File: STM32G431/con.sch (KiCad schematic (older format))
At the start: 64 parts, among them J10 NTC, J11 LED, J4 GND, J5 VIN, J6 UART, J7 ENCODER, J8 HALL, J9 AIN, P1 TC2030-CTX-Tag-Connect, Q2 Q_NMOS_GSD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

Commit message: updated files
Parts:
- removed D18, D19: SS310, Diode_SMD:D_SOD-123F, symbol Device:D_Small
- removed J7: ENCODER, Connector_Molex:Molex_PicoBlade_53261-0671_1x06-1MP_P1.25mm_Horizontal, symbol Connector_Generic_MountingPin:Conn_01x06_MountingPin
- removed J9: AIN, Connector_Molex:Molex_PicoBlade_53261-0371_1x03-1MP_P1.25mm_Horizontal, symbol Connector_Generic_MountingPin:Conn_01x03_MountingPin
- removed R18, R22: 120, Resistor_SMD:R_0603_1608Metric, symbol Device:R_Small
- removed U6: ENCODER A, Package_SO:SOIC-8_3.9x4.9mm_P1.27mm, symbol otter:RS485
- removed U7: ENCODER B, Package_SO:SOIC-8_3.9x4.9mm_P1.27mm, symbol otter:RS485
- added D14, D15: SM4007PL, Diode_SMD:D_SOD-123F, symbol Device:D_Small
- added D2, D5: B5819W, Diode_SMD:D_SOD-123, symbol Device:D_Schottky
- added J9: AIN/PWM, Connector_Molex:Molex_PicoBlade_53261-0471_1x04-1MP_P1.25mm_Horizontal, symbol Connector_Generic_MountingPin:Conn_01x04_MountingPin
- gave numbers to parts that had none: 4
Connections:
- net +3V3: now also D2.1 (K)
- net CANRX: no longer R5.2, U11.1 (IO1), U5.1 (DI)
- net CANTX: no longer R4.2, U11.3 (IO2), U5.4 (DO)
- net GND: now also D14.2 (A), J9.4 (Pin_4), J9.MP (MountPin); no longer R24.2
- net GPIO_BEMF: now also D5.1 (K)
- net NTC_EXT: now also D15.2 (A)
- net UU: now also R24.2, D2.2 (A); no longer R24.1
- net UV: now also D6.2 (A)
- net VIO: now also J9.1 (Pin_1)
- net at R45.2, R46.2: now also J9.3 (Pin_3)
- net at C40.1, Q2.1 (G), R21.1: now also D15.1 (K)
- net at C35.2, L1.1, U3.1 (SW): now also D14.1 (K)
- new net: D5.2 (A), R24.1
- new net PWM: J9.2 (Pin_2), U11.3 (IO2)
- new net UART_RX: R4.2, U5.4 (DO)
- new net UART_TX: R5.2, U5.1 (DI)
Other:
- moved on the sheet: C29, D10, D13, D6, D7, R23, R24, R26, R31, U5

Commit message: updated files
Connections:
- net NTC_EXT: now also U9.4 (IO3); no longer U8.6 (IO4)
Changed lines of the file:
@@
 Text GLabel 9550 3400 0    50   Input ~ 0
 SWDIO
-Text GLabel 10150 3500 2    50   Input ~ 0
+Text GLabel 10150 4300 2    50   Input ~ 0
 NTC_POWERSTAGE
 Text GLabel 10150 4900 2    50   Input ~ 0

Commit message: updated files
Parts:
- R27, R28, R29: value 100 -> 1.8k
- R33, R34, R35: value 1k -> 10k
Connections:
- net VIO is gone; now on net +3V3: J9.1 (Pin_1), JP2.1 (A), P1.1 (VCC), R33.1, R34.1, R35.1, R46.1
- net VP renamed +12V
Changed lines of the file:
@@
 AR Path="/5D59ABFE/5D5B747D" Ref="R35"  Part="1"
 F 0 "R35" H 6458 1704 50  0000 L CNN
-F 1 "1k" H 6458 1795 50  0000 L CNN
+F 1 "10k" H 6458 1795 50  0000 L CNN
 F 2 "Resistor_SMD:R_0603_1608Metric" H 6400 1750 50  0001 C CNN
 F 3 "~" H 6400 1750 50  0001 C CNN
@@
 AR Path="/5D59ABFE/5D5B7483" Ref="R34"  Part="1"
 F 0 "R34" H 6600 2100 50  0000 R CNN
-F 1 "1k" H 6550 1950 50  0000 R CNN
+F 1 "10k" H 6550 1950 50  0000 R CNN
 F 2 "Resistor_SMD:R_0603_1608Metric" H 6500 1750 50  0001 C CNN
 F 3 "~" H 6500 1750 50  0001 C CNN
@@
 AR Path="/5D59ABFE/5D5B7489" Ref="R33"  Part="1"
 F 0 "R33" H 6541 1704 50  0000 R CNN
-F 1 "1k" H 6541 1795 50  0000 R CNN
+F 1 "10k" H 6541 1795 50  0000 R CNN
 F 2 "Resistor_SMD:R_0603_1608Metric" H 6600 1750 50  0001 C CNN
 F 3 "~" H 6600 1750 50  0001 C CNN
@@
 AR Path="/5D59ABFE/5D5B757B" Ref="R28"  Part="1"
 F 0 "R28" V 6200 750 50  0000 C CNN
-F 1 "100" V 6300 750 50  0000 C CNN
+F 1 "1.8k" V 6300 750 50  0000 C CNN
 F 2 "Resistor_SMD:R_0603_1608Metric" H 6250 1200 50  0001 C CNN
 F 3 "~" H 6250 1200 50  0001 C CNN
@@
 AR Path="/5D59ABFE/5D5B7581" Ref="R27"  Part="1"
 F 0 "R27" V 6054 1100 50  0000 C CNN
-F 1 "100" V 6145 1100 50  0000 C CNN
+F 1 "1.8k" V 6145 1100 50  0000 C CNN
 F 2 "Resistor_SMD:R_0603_1608Metric" H 6250 1100 50  0001 C CNN
 F 3 "~" H 6250 1100 50  0001 C CNN
@@
 AR Path="/5D59ABFE/5D5B758B" Ref="R29"  Part="1"
 F 0 "R29" V 6354 1300 50  0000 C CNN
-F 1 "100" V 6445 1300 50  0000 C CNN
+F 1 "1.8k" V 6445 1300 50  0000 C CNN
 F 2 "Resistor_SMD:R_0603_1608Metric" H 6250 1300 50  0001 C CNN
 F 3 "~" H 6250 1300 50  0001 C CNN
@@
 Wire Wire Line
 	7700 1100 7850 1100
-Text GLabel 4850 850  0    50   Input ~ 0
-VIO
 Wire Wire Line
 	6400 1650 6400 1100
@@
 	1    0    0    -1
 $EndComp
-Text GLabel 1850 7050 0    50   Input ~ 0
-VIO
 $Comp
 L power:GND #PWR?
@@
 Text GLabel 4150 4450 1    50   Input ~ 0
 3V3
-Text GLabel 7850 900  0    50   Input ~ 0
-VIO
-Text GLabel 7700 1300 3    50   Input ~ 0
-VIO
-Text GLabel 6400 1850 3    50   Input ~ 0
-VIO
 $Comp
 L Device:R_Small R?
@@
 	1    0    0    -1
 $EndComp
-Text GLabel 3600 2850 0    50   Input ~ 0
-VP
 $Comp
 L power:GND #PWR0156
@@
 Wire Wire Line
 	4150 5200 4550 5200
+$Comp
+L power:+3.3V #PWR0212
+U 1 1 5DEBC23B
+P 6400 1900
+F 0 "#PWR0212" H 6400 1750 50  0001 C CNN
+F 1 "+3.3V" H 6415 2073 50  0000 C CNN
+F 2 "" H 6400 1900 50  0001 C CNN
+F 3 "" H 6400 1900 50  0001 C CNN
+	1    6400 1900
+	-1   0    0    1
+$EndComp
+Wire Wire Line
+	6400 1900 6400 1850
+Connection ~ 6400 1850
+$Comp
+L power:+3.3V #PWR0213
+U 1 1 5DEC0D60
+P 4850 850
+F 0 "#PWR0213" H 4850 700 50  0001 C CNN
+F 1 "+3.3V" H 4865 1023 50  0000 C CNN
+F 2 "" H 4850 850 50  0001 C CNN
+F 3 "" H 4850 850 50  0001 C CNN
+	1    4850 850
+	0    -1   -1   0
+$EndComp
+$Comp
+L power:+3.3V #PWR0214
+U 1 1 5DEC82F1
+P 7850 900
+F 0 "#PWR0214" H 7850 750 50  0001 C CNN
+F 1 "+3.3V" H 7865 1073 50  0000 C CNN
+F 2 "" H 7850 900 50  0001 C CNN
+F 3 "" H 7850 900 50  0001 C CNN
+	1    7850 900
+	0    -1   -1   0
+$EndComp
+$Comp
+L power:+3.3V #PWR0215
+U 1 1 5DEC9F93
+P 7700 1300
+F 0 "#PWR0215" H 7700 1150 50  0001 C CNN
+F 1 "+3.3V" H 7715 1473 50  0000 C CNN
+F 2 "" H 7700 1300 50  0001 C CNN
+F 3 "" H 7700 1300 50  0001 C CNN
+	1    7700 1300
+	-1   0    0    1
+$EndComp
+$Comp
+L power:+3.3V #PWR0216
+U 1 1 5DED00F0
+P 1850 7050
+F 0 "#PWR0216" H 1850 6900 50  0001 C CNN
+F 1 "+3.3V" H 1865 7223 50  0000 C CNN
+F 2 "" H 1850 7050 50  0001 C CNN
+F 3 "" H 1850 7050 50  0001 C CNN
+	1    1850 7050
+	0    -1   -1   0
+$EndComp
+$Comp
+L power:+12V #PWR0217
+U 1 1 5DED744B
+P 3600 2850
+F 0 "#PWR0217" H 3600 2700 50  0001 C CNN
+F 1 "+12V" H 3615 3023 50  0000 C CNN
+F 2 "" H 3600 2850 50  0001 C CNN
+F 3 "" H 3600 2850 50  0001 C CNN
+	1    3600 2850
+	1    0    0    -1
+$EndComp
 $EndSCHEMATC

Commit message: updated files
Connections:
- net SWDCL is gone; now on net SWCLK: U8.3 (IO2)
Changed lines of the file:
@@
 $EndComp
 Text GLabel 9550 3500 0    50   Input ~ 0
-SWDCL
+SWCLK
 Text GLabel 9550 3400 0    50   Input ~ 0
 SWDIO

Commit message: remaned files
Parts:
- removed D14, D15: SM4007PL, Diode_SMD:D_SOD-123F, symbol Device:D_Small
- added D? (x2): B5819W, Diode_SMD:D_SOD-123, symbol Device:D_Schottky
- C29, C30, C31, C42: footprint Capacitor_SMD:C_0603_1608Metric -> Capacitor_SMD:C_0402_1005Metric
- C39, C40: footprint Capacitor_SMD:C_0603_1608Metric -> Resistor_SMD:R_0402_1005Metric
- R17, R6: footprint Resistor_SMD:R_0603_1608Metric -> Capacitor_SMD:C_0402_1005Metric
- R20, R21, R27, R28, R29, R32, R33, R34, R35, R37, R38, R39, R4, R45, R46, R5: footprint Resistor_SMD:R_0603_1608Metric -> Resistor_SMD:R_0402_1005Metric
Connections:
- net 3V3 is gone; now on net +3V3: R20.1
- net GND: now also D?.2 (A)
- net NTC_EXT: now also D?.2 (A)
- net at C40.1, Q2.1 (G), R21.1: now also D?.1 (K)
- net at C35.2, L1.1, U3.1 (SW): now also D?.1 (K)
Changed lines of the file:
@@
 EESchema Schematic File Version 4
-LIBS:PAC5523-cache
+LIBS:STM32G431-cache
 EELAYER 30 0
 EELAYER END
@@
 F 0 "R35" H 6458 1704 50  0000 L CNN
 F 1 "10k" H 6458 1795 50  0000 L CNN
-F 2 "Resistor_SMD:R_0603_1608Metric" H 6400 1750 50  0001 C CNN
+F 2 "Resistor_SMD:R_0402_1005Metric" H 6400 1750 50  0001 C CNN
 F 3 "~" H 6400 1750 50  0001 C CNN
 	1    6400 1750
@@
 F 0 "R34" H 6600 2100 50  0000 R CNN
 F 1 "10k" H 6550 1950 50  0000 R CNN
-F 2 "Resistor_SMD:R_0603_1608Metric" H 6500 1750 50  0001 C CNN
+F 2 "Resistor_SMD:R_0402_1005Metric" H 6500 1750 50  0001 C CNN
 F 3 "~" H 6500 1750 50  0001 C CNN
 	1    6500 1750
@@
 F 0 "R33" H 6541 1704 50  0000 R CNN
 F 1 "10k" H 6541 1795 50  0000 R CNN
-F 2 "Resistor_SMD:R_0603_1608Metric" H 6600 1750 50  0001 C CNN
+F 2 "Resistor_SMD:R_0402_1005Metric" H 6600 1750 50  0001 C CNN
 F 3 "~" H 6600 1750 50  0001 C CNN
 	1    6600 1750
@@
 F 0 "C31" H 6092 7246 50  0000 L CNN
 F 1 "100p" H 6092 7155 50  0000 L CNN
-F 2 "Capacitor_SMD:C_0603_1608Metric" H 6000 7200 50  0001 C CNN
+F 2 "Capacitor_SMD:C_0402_1005Metric" H 6000 7200 50  0001 C CNN
 F 3 "~" H 6000 7200 50  0001 C CNN
 	1    6000 7200
@@
 F 0 "C30" H 4892 7246 50  0000 L CNN
 F 1 "100p" H 4892 7155 50  0000 L CNN
-F 2 "Capacitor_SMD:C_0603_1608Metric" H 4800 7200 50  0001 C CNN
+F 2 "Capacitor_SMD:C_0402_1005Metric" H 4800 7200 50  0001 C CNN
 F 3 "~" H 4800 7200 50  0001 C CNN
 	1    4800 7200
@@
 F 0 "C29" H 3742 7246 50  0000 L CNN
 F 1 "100p" H 3742 7155 50  0000 L CNN
-F 2 "Capacitor_SMD:C_0603_1608Metric" H 3650 7200 50  0001 C CNN
+F 2 "Capacitor_SMD:C_0402_1005Metric" H 3650 7200 50  0001 C CNN
 F 3 "~" H 3650 7200 50  0001 C CNN
 	1    3650 7200
@@
 F 0 "R39" V 3704 5200 50  0000 C CNN
 F 1 "100" V 3795 5200 50  0000 C CNN
-F 2 "Resistor_SMD:R_0603_1608Metric" H 3900 5200 50  0001 C CNN
+F 2 "Resistor_SMD:R_0402_1005Metric" H 3900 5200 50  0001 C CNN
 F 3 "~" H 3900 5200 50  0001 C CNN
 	1    3900 5200
@@
 F 0 "R28" V 6200 750 50  0000 C CNN
 F 1 "1.8k" V 6300 750 50  0000 C CNN
-F 2 "Resistor_SMD:R_0603_1608Metric" H 6250 1200 50  0001 C CNN
+F 2 "Resistor_SMD:R_0402_1005Metric" H 6250 1200 50  0001 C CNN
 F 3 "~" H 6250 1200 50  0001 C CNN
 	1    6250 1200
@@
 F 0 "R27" V 6054 1100 50  0000 C CNN
 F 1 "1.8k" V 6145 1100 50  0000 C CNN
-F 2 "Resistor_SMD:R_0603_1608Metric" H 6250 1100 50  0001 C CNN
+F 2 "Resistor_SMD:R_0402_1005Metric" H 6250 1100 50  0001 C CNN
 F 3 "~" H 6250 1100 50  0001 C CNN
 	1    6250 1100
@@
 F 0 "R29" V 6354 1300 50  0000 C CNN
 F 1 "1.8k" V 6445 1300 50  0000 C CNN
-F 2 "Resistor_SMD:R_0603_1608Metric" H 6250 1300 50  0001 C CNN
+F 2 "Resistor_SMD:R_0402_1005Metric" H 6250 1300 50  0001 C CNN
 F 3 "~" H 6250 1300 50  0001 C CNN
 	1    6250 1300
@@
 F 0 "R5" V 4304 1200 50  0000 C CNN
 F 1 "100" V 4395 1200 50  0000 C CNN
-F 2 "Resistor_SMD:R_0603_1608Metric" H 4200 1200 50  0001 C CNN
+F 2 "Resistor_SMD:R_0402_1005Metric" H 4200 1200 50  0001 C CNN
 F 3 "~" H 4200 1200 50  0001 C CNN
 	1    4200 1200
@@
 F 0 "R4" V 4004 1100 50  0000 C CNN
 F 1 "100" V 4095 1100 50  0000 C CNN
-F 2 "Resistor_SMD:R_0603_1608Metric" H 4200 1100 50  0001 C CNN
+F 2 "Resistor_SMD:R_0402_1005Metric" H 4200 1100 50  0001 C CNN
 F 3 "~" H 4200 1100 50  0001 C CNN
 	1    4200 1100
@@
 F 0 "R45" V 7304 1100 50  0000 C CNN
 F 1 "100" V 7395 1100 50  0000 C CNN
-F 2 "Resistor_SMD:R_0603_1608Metric" H 7500 1100 50  0001 C CNN
+F 2 "Resistor_SMD:R_0402_1005Metric" H 7500 1100 50  0001 C CNN
 F 3 "~" H 7500 1100 50  0001 C CNN
 	1    7500 1100
@@
 F 0 "R46" H 7750 1650 50  0000 R CNN
 F 1 "1k" H 7750 1550 50  0000 R CNN
-F 2 "Resistor_SMD:R_0603_1608Metric" H 7700 1200 50  0001 C CNN
+F 2 "Resistor_SMD:R_0402_1005Metric" H 7700 1200 50  0001 C CNN
 F 3 "~" H 7700 1200 50  0001 C CNN
 	1    7700 1200
@@
 F 0 "R21" H 5309 5346 50  0000 L CNN
 F 1 "1M" H 5309 5255 50  0000 L CNN
-F 2 "Resistor_SMD:R_0603_1608Metric" H 5250 5300 50  0001 C CNN
+F 2 "Resistor_SMD:R_0402_1005Metric" H 5250 5300 50  0001 C CNN
 F 3 "~" H 5250 5300 50  0001 C CNN
 	1    5250 5300
@@
 F 0 "C39" H 4242 5346 50  0000 L CNN
 F 1 "100p" H 4242 5255 50  0000 L CNN
-F 2 "Capacitor_SMD:C_0603_1608Metric" H 4150 5300 50  0001 C CNN
+F 2 "Resistor_SMD:R_0402_1005Metric" H 4150 5300 50  0001 C CNN
 F 3 "~" H 4150 5300 50  0001 C CNN
 	1    4150 5300
@@
 F 0 "C40" H 4992 5346 50  0000 L CNN
 F 1 "100p" H 4992 5255 50  0000 L CNN
-F 2 "Capacitor_SMD:C_0603_1608Metric" H 4900 5300 50  0001 C CNN
+F 2 "Resistor_SMD:R_0402_1005Metric" H 4900 5300 50  0001 C CNN
 F 3 "~" H 4900 5300 50  0001 C CNN
 	1    4900 5300
@@
 Connection ~ 4900 5200
 Wire Wire Line
-	4900 5200 4750 5200
+	4900 5200 4800 5200
 $Comp
 L power:GND #PWR?
@@
 F 0 "R20" H 4209 4596 50  0000 L CNN
 F 1 "47k" H 4209 4505 50  0000 L CNN
-F 2 "Resistor_SMD:R_0603_1608Metric" H 4150 4550 50  0001 C CNN
+F 2 "Resistor_SMD:R_0402_1005Metric" H 4150 4550 50  0001 C CNN
 F 3 "~" H 4150 4550 50  0001 C CNN
 	1    4150 4550
@@
 	0    -1   -1   0
 $EndComp
-Text GLabel 4150 4450 1    50   Input ~ 0
-3V3
 $Comp
 L Device:R_Small R?
@@
 F 0 "R6" H 7809 5896 50  0000 L CNN
 F 1 "100k" H 7809 5805 50  0000 L CNN
-F 2 "Resistor_SMD:R_0603_1608Metric" H 7750 5850 50  0001 C CNN
+F 2 "Capacitor_SMD:C_0402_1005Metric" H 7750 5850 50  0001 C CNN
 F 3 "~" H 7750 5850 50  0001 C CNN
 	1    7750 5850
@@
 F 0 "R17" H 7809 6196 50  0000 L CNN
 F 1 "4k3" H 7809 6105 50  0000 L CNN
-F 2 "Resistor_SMD:R_0603_1608Metric" H 7750 6150 50  0001 C CNN
+F 2 "Capacitor_SMD:C_0402_1005Metric" H 7750 6150 50  0001 C CNN
 F 3 "~" H 7750 6150 50  0001 C CNN
 	1    7750 6150
@@
 F 0 "C42" H 7542 6196 50  0000 L CNN
 F 1 "100p" H 7542 6105 50  0000 L CNN
-F 2 "Capacitor_SMD:C_0603_1608Metric" H 7450 6150 50  0001 C CNN
+F 2 "Capacitor_SMD:C_0402_1005Metric" H 7450 6150 50  0001 C CNN
 F 3 "~" H 7450 6150 50  0001 C CNN
 	1    7450 6150
@@
 F 0 "R38" H 5209 3496 50  0000 L CNN
 F 1 "9k1" H 5209 3405 50  0000 L CNN
-F 2 "Resistor_SMD:R_0603_1608Metric" H 5150 3450 50  0001 C CNN
+F 2 "Resistor_SMD:R_0402_1005Metric" H 5150 3450 50  0001 C CNN
 F 3 "~" H 5150 3450 50  0001 C CNN
 	1    5150 3450
@@
 F 0 "R37" H 5209 3196 50  0000 L CNN
 F 1 "47k" H 5209 3105 50  0000 L CNN
-F 2 "Resistor_SMD:R_0603_1608Metric" H 5150 3150 50  0001 C CNN
+F 2 "Resistor_SMD:R_0402_1005Metric" H 5150 3150 50  0001 C CNN
 F 3 "~" H 5150 3150 50  0001 C CNN
 	1    5150 3150
@@
 L power:GND #PWR0155
 U 1 1 5CEAAA67
-P 4550 3500
-F 0 "#PWR0155" H 4550 3250 50  0001 C CNN
-F 1 "GND" H 4555 3327 50  0000 C CNN
-F 2 "" H 4550 3500 50  0001 C CNN
-F 3 "" H 4550 3500 50  0001 C CNN
-	1    4550 3500
+P 4550 3600
+F 0 "#PWR0155" H 4550 3350 50  0001 C CNN
+F 1 "GND" H 4555 3427 50  0000 C CNN
+F 2 "" H 4550 3600 50  0001 C CNN
+F 3 "" H 4550 3600 50  0001 C CNN
+	1    4550 3600
 	1    0    0    -1
 $EndComp
@@
 F 0 "R32" H 1009 5196 50  0000 L CNN
 F 1 "4k3" H 1009 5105 50  0000 L CNN
-F 2 "Resistor_SMD:R_0603_1608Metric" H 950 5150 50  0001 C CNN
+F 2 "Resistor_SMD:R_0402_1005Metric" H 950 5150 50  0001 C CNN
 F 3 "~" H 950 5150 50  0001 C CNN
 	1    950  5150
@@
 UART_RX
 $Comp
-L Device:D_Small D?
-U 1 1 5DF35224
-P 4550 3400
-AR Path="/5DF35224" Ref="D?"  Part="1"
-AR Path="/5D59ABFE/5DF35224" Ref="D14"  Part="1"
-F 0 "D14" V 4504 3468 50  0000 L CNN
-F 1 "SM4007PL" V 4595 3468 50  0000 L CNN
-F 2 "Diode_SMD:D_SOD-123F" V 4550 3400 50  0001 C CNN
-F 3 "~" V 4550 3400 50  0001 C CNN
-	1    4550 3400
-	0    1    1    0
-$EndComp
-$Comp
-L Device:D_Small D?
-U 1 1 5DF3CAC5
-P 4650 5200
-AR Path="/5DF3CAC5" Ref="D?"  Part="1"
-AR Path="/5D59ABFE/5DF3CAC5" Ref="D15"  Part="1"
-F 0 "D15" V 4604 5268 50  0000 L CNN
-F 1 "SM4007PL" V 4695 5268 50  0000 L CNN
-F 2 "Diode_SMD:D_SOD-123F" V 4650 5200 50  0001 C CNN
-F 3 "~" V 4650 5200 50  0001 C CNN
-	1    4650 5200
-	-1   0    0    1
-$EndComp
-Wire Wire Line
-	4150 5200 4550 5200
-$Comp
 L power:+3.3V #PWR0212
 U 1 1 5DEBC23B
@@
 	1    0    0    -1
 $EndComp
+$Comp
+L power:+3.3V #PWR?
+U 1 1 5E0AF941
+P 4150 4450
+F 0 "#PWR?" H 4150 4300 50  0001 C CNN
+F 1 "+3.3V" H 4165 4623 50  0000 C CNN
+F 2 "" H 4150 4450 50  0001 C CNN
+F 3 "" H 4150 4450 50  0001 C CNN
+	1    4150 4450
+	1    0    0    -1
+$EndComp
+Wire Wire Line
+	4150 5200 4500 5200
+$Comp
+L Device:D_Schottky D?
+U 1 1 5DFB1AE0
+P 4650 5200
+F 0 "D?" V 4604 5279 50  0000 L CNN
+F 1 "B5819W" V 4695 5279 50  0000 L CNN
+F 2 "Diode_SMD:D_SOD-123" H 4650 5200 50  0001 C CNN
+F 3 "https://datasheet.lcsc.com/szlcsc/Changjiang-Electronics-Tech-CJ-B5819W_C8598.pdf" H 4650 5200 50  0001 C CNN
+F 4 "C8598" H 4650 5200 50  0001 C CNN "LCSC"
+	1    4650 5200
+	-1   0    0    1
+$EndComp
+$Comp
+L Device:D_Schottky D?
+U 1 1 5DFBDED8
+P 4550 3450
+F 0 "D?" V 4504 3529 50  0000 L CNN
+F 1 "B5819W" V 4595 3529 50  0000 L CNN
+F 2 "Diode_SMD:D_SOD-123" H 4550 3450 50  0001 C CNN
+F 3 "https://datasheet.lcsc.com/szlcsc/Changjiang-Electronics-Tech-CJ-B5819W_C8598.pdf" H 4550 3450 50  0001 C CNN
+F 4 "C8598" H 4550 3450 50  0001 C CNN "LCSC"
+	1    4550 3450
+	0    1    1    0
+$EndComp
 $EndSCHEMATC

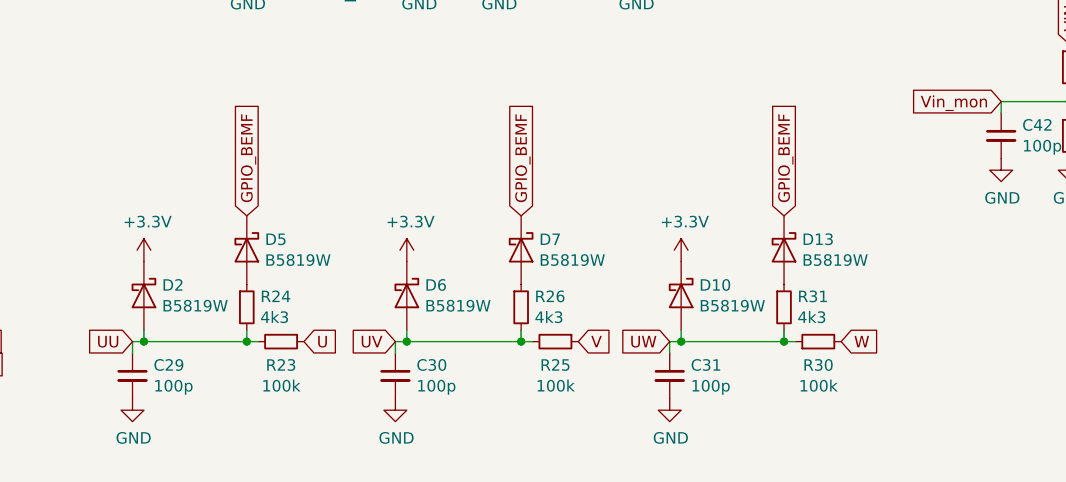
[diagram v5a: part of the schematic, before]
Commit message: updated layout
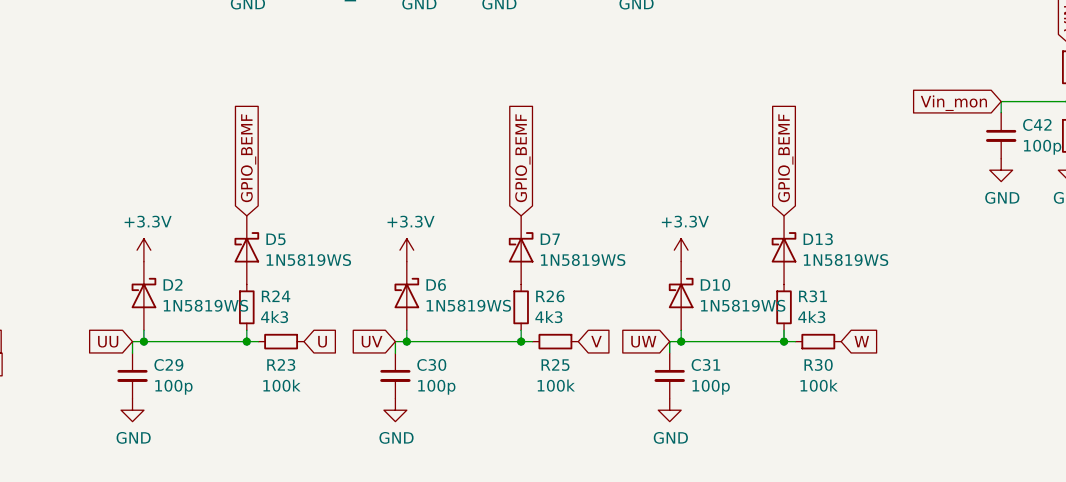
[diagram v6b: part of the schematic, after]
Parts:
- D10, D13, D2, D5, D6, D7: value B5819W -> 1N5819WS; footprint Diode_SMD:D_SOD-123 -> Diode_SMD:D_SOD-323
- R23, R24, R25, R26, R30, R31: footprint Resistor_SMD:R_0603_1608Metric -> Resistor_SMD:R_0402_1005Metric
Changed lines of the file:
@@
 F 0 "R30" V 6546 7050 50  0000 C CNN
 F 1 "100k" V 6455 7050 50  0000 C CNN
-F 2 "Resistor_SMD:R_0603_1608Metric" H 6650 7050 50  0001 C CNN
+F 2 "Resistor_SMD:R_0402_1005Metric" H 6650 7050 50  0001 C CNN
 F 3 "~" H 6650 7050 50  0001 C CNN
 	1    6650 7050
@@
 F 0 "R31" H 6559 6946 50  0000 L CNN
 F 1 "4k3" H 6559 6855 50  0000 L CNN
-F 2 "Resistor_SMD:R_0603_1608Metric" H 6500 6900 50  0001 C CNN
+F 2 "Resistor_SMD:R_0402_1005Metric" H 6500 6900 50  0001 C CNN
 F 3 "~" H 6500 6900 50  0001 C CNN
 	1    6500 6900
@@
 F 0 "R25" V 5604 7050 50  0000 C CNN
 F 1 "100k" V 5695 7050 50  0000 C CNN
-F 2 "Resistor_SMD:R_0603_1608Metric" H 5500 7050 50  0001 C CNN
+F 2 "Resistor_SMD:R_0402_1005Metric" H 5500 7050 50  0001 C CNN
 F 3 "~" H 5500 7050 50  0001 C CNN
 	1    5500 7050
@@
 F 0 "R23" V 4404 7050 50  0000 C CNN
 F 1 "100k" V 4495 7050 50  0000 C CNN
-F 2 "Resistor_SMD:R_0603_1608Metric" H 4300 7050 50  0001 C CNN
+F 2 "Resistor_SMD:R_0402_1005Metric" H 4300 7050 50  0001 C CNN
 F 3 "~" H 4300 7050 50  0001 C CNN
 	1    4300 7050
@@
 F 0 "R24" H 4209 6946 50  0000 L CNN
 F 1 "4k3" H 4209 6855 50  0000 L CNN
-F 2 "Resistor_SMD:R_0603_1608Metric" H 4150 6900 50  0001 C CNN
+F 2 "Resistor_SMD:R_0402_1005Metric" H 4150 6900 50  0001 C CNN
 F 3 "~" H 4150 6900 50  0001 C CNN
 	1    4150 6900
@@
 P 6050 6850
 F 0 "D10" V 6004 6929 50  0000 L CNN
-F 1 "B5819W" V 6095 6929 50  0000 L CNN
-F 2 "Diode_SMD:D_SOD-123" H 6050 6850 50  0001 C CNN
+F 1 "1N5819WS" V 6095 6929 50  0000 L CNN
+F 2 "Diode_SMD:D_SOD-323" H 6050 6850 50  0001 C CNN
 F 3 "https://datasheet.lcsc.com/szlcsc/Changjiang-Electronics-Tech-CJ-B5819W_C8598.pdf" H 6050 6850 50  0001 C CNN
 F 4 "C8598" H 6050 6850 50  0001 C CNN "LCSC"
@@
 P 6500 6650
 F 0 "D13" V 6454 6729 50  0000 L CNN
-F 1 "B5819W" V 6545 6729 50  0000 L CNN
-F 2 "Diode_SMD:D_SOD-123" H 6500 6650 50  0001 C CNN
+F 1 "1N5819WS" V 6545 6729 50  0000 L CNN
+F 2 "Diode_SMD:D_SOD-323" H 6500 6650 50  0001 C CNN
 F 3 "https://datasheet.lcsc.com/szlcsc/Changjiang-Electronics-Tech-CJ-B5819W_C8598.pdf" H 6500 6650 50  0001 C CNN
 F 4 "C8598" H 6500 6650 50  0001 C CNN "LCSC"
@@
 P 4850 6850
 F 0 "D6" V 4804 6929 50  0000 L CNN
-F 1 "B5819W" V 4895 6929 50  0000 L CNN
-F 2 "Diode_SMD:D_SOD-123" H 4850 6850 50  0001 C CNN
+F 1 "1N5819WS" V 4895 6929 50  0000 L CNN
+F 2 "Diode_SMD:D_SOD-323" H 4850 6850 50  0001 C CNN
 F 3 "https://datasheet.lcsc.com/szlcsc/Changjiang-Electronics-Tech-CJ-B5819W_C8598.pdf" H 4850 6850 50  0001 C CNN
 F 4 "C8598" H 4850 6850 50  0001 C CNN "LCSC"
@@
 F 0 "R26" H 5409 6946 50  0000 L CNN
 F 1 "4k3" H 5409 6855 50  0000 L CNN
-F 2 "Resistor_SMD:R_0603_1608Metric" H 5350 6900 50  0001 C CNN
+F 2 "Resistor_SMD:R_0402_1005Metric" H 5350 6900 50  0001 C CNN
 F 3 "~" H 5350 6900 50  0001 C CNN
 	1    5350 6900
@@
 P 5350 6650
 F 0 "D7" V 5304 6729 50  0000 L CNN
-F 1 "B5819W" V 5395 6729 50  0000 L CNN
-F 2 "Diode_SMD:D_SOD-123" H 5350 6650 50  0001 C CNN
+F 1 "1N5819WS" V 5395 6729 50  0000 L CNN
+F 2 "Diode_SMD:D_SOD-323" H 5350 6650 50  0001 C CNN
 F 3 "https://datasheet.lcsc.com/szlcsc/Changjiang-Electronics-Tech-CJ-B5819W_C8598.pdf" H 5350 6650 50  0001 C CNN
 F 4 "C8598" H 5350 6650 50  0001 C CNN "LCSC"
@@
 P 3700 6850
 F 0 "D2" V 3654 6929 50  0000 L CNN
-F 1 "B5819W" V 3745 6929 50  0000 L CNN
-F 2 "Diode_SMD:D_SOD-123" H 3700 6850 50  0001 C CNN
+F 1 "1N5819WS" V 3745 6929 50  0000 L CNN
+F 2 "Diode_SMD:D_SOD-323" H 3700 6850 50  0001 C CNN
 F 3 "https://datasheet.lcsc.com/szlcsc/Changjiang-Electronics-Tech-CJ-B5819W_C8598.pdf" H 3700 6850 50  0001 C CNN
 F 4 "C8598" H 3700 6850 50  0001 C CNN "LCSC"
@@
 P 4150 6650
 F 0 "D5" V 4104 6729 50  0000 L CNN
-F 1 "B5819W" V 4195 6729 50  0000 L CNN
-F 2 "Diode_SMD:D_SOD-123" H 4150 6650 50  0001 C CNN
+F 1 "1N5819WS" V 4195 6729 50  0000 L CNN
+F 2 "Diode_SMD:D_SOD-323" H 4150 6650 50  0001 C CNN
 F 3 "https://datasheet.lcsc.com/szlcsc/Changjiang-Electronics-Tech-CJ-B5819W_C8598.pdf" H 4150 6650 50  0001 C CNN
 F 4 "C8598" H 4150 6650 50  0001 C CNN "LCSC"
